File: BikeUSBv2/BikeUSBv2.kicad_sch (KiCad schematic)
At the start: 48 parts, among them J1 TYPE-C-31-M-16, J2 Conn_01x02_Female, Q1 SSM3J332R,LF, Q2 SSM3J332R,LF, SW1 SW_Push, SW2 SW_Push, U1 TPS63020DSJR, U2 ATtiny1616-M

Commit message: added pcb art, other stuff
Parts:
- L1: value 1u -> YPRH0704-1R0M; Alternative (none) -> YPRH0704-2R2M; LCSC Part (none) -> C338840
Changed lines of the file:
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@@
-    (stroke (width 0) (type default))
-  )
-  (wire (pts (xy 78.105 95.885) (xy 70.485 95.885))
     (stroke (width 0) (type default))
   )
@@
   )
   (wire (pts (xy 41.91 88.265) (xy 35.56 88.265))
+    (stroke (width 0) (type default))
+  )
+  (wire (pts (xy 70.485 95.885) (xy 78.105 95.885))
     (stroke (width 0) (type default))
   )
@@
       (effects (font (size 1.27 1.27)))
     )
-    (property "Value" "1u" (at 74.295 100.33 90)
+    (property "Value" "YPRH0704-1R0M" (at 74.295 100.965 90)
       (effects (font (size 1.27 1.27)))
     )
@@
       (effects (font (size 1.27 1.27)) hide)
     )
+    (property "LCSC Part" "C338840" (at 74.295 99.695 90)
+      (effects (font (size 1.27 1.27)) hide)
+    )
+    (property "Alternative" "YPRH0704-2R2M" (at 74.295 99.695 90)
+      (effects (font (size 1.27 1.27)) hide)
+    )

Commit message: small stuff
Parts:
- added TP7: EN, TestPoint:TestPoint_Pad_D2.5mm, symbol Connector:TestPoint
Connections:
- net EN: now also TP7.1
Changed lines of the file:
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@@
+    (stroke (width 0) (type default))
+  )
+  (wire (pts (xy 25.4 172.085) (xy 22.225 172.085))
     (stroke (width 0) (type default))
   )
@@
     (effects (font (size 1.27 1.27)) (justify right bottom))
   )
+  (label "EN" (at 25.4 172.085 180) (fields_autoplaced)
+    (effects (font (size 1.27 1.27)) (justify right bottom))
+  )
   (label "AC1" (at 77.47 111.125 270) (fields_autoplaced)
     (effects (font (size 1.27 1.27)) (justify right bottom))
@@
         )
       )
+    )
+  )
+  (symbol (lib_id "Connector:TestPoint") (at 22.225 172.085 90) (unit 1)
+    (in_bom yes) (on_board yes) (dnp no)
+    (property "Reference" "TP7" (at 20.193 174.625 0)
+      (effects (font (size 1.27 1.27)) (justify right) hide)
+    )
+    (property "Value" "EN" (at 14.605 172.085 90)
+      (effects (font (size 1.27 1.27)) (justify right))
+    )
+    (property "Footprint" "TestPoint:TestPoint_Pad_D2.5mm" (at 22.225 167.005 0)
+      (effects (font (size 1.27 1.27)) hide)
+    )
+    (property "Datasheet" "~" (at 22.225 167.005 0)
+      (effects (font (size 1.27 1.27)) hide)
+    )
+    (pin "1")
+    (instances
+      (project "BikeUSBv2"
+        (path "/b4aff538-5116-4944-9d24-c26a88d7dfe8"
+          (reference "TP7") (unit 1)
+        )
+      )

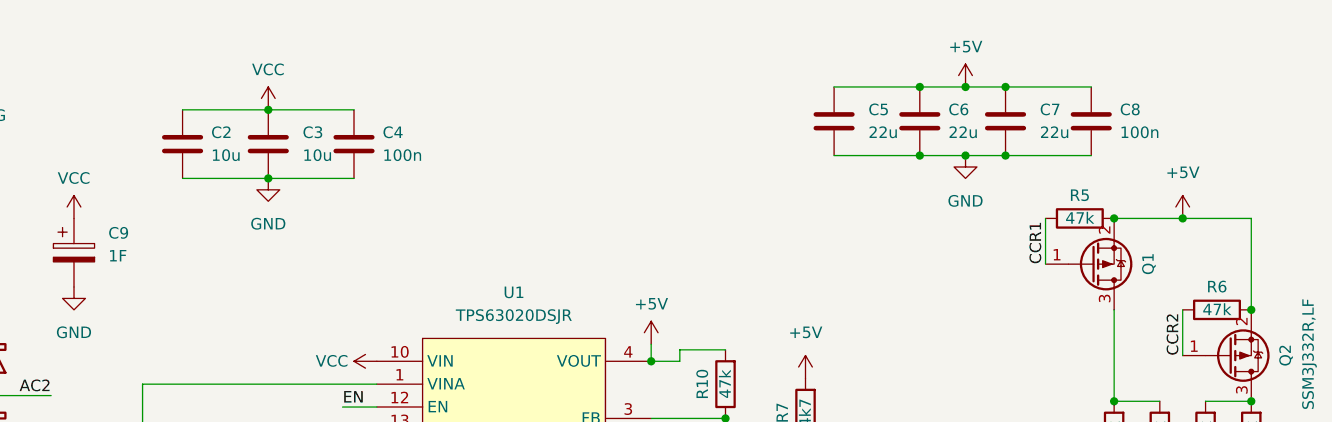
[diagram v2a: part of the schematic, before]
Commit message: better U1 cap layout
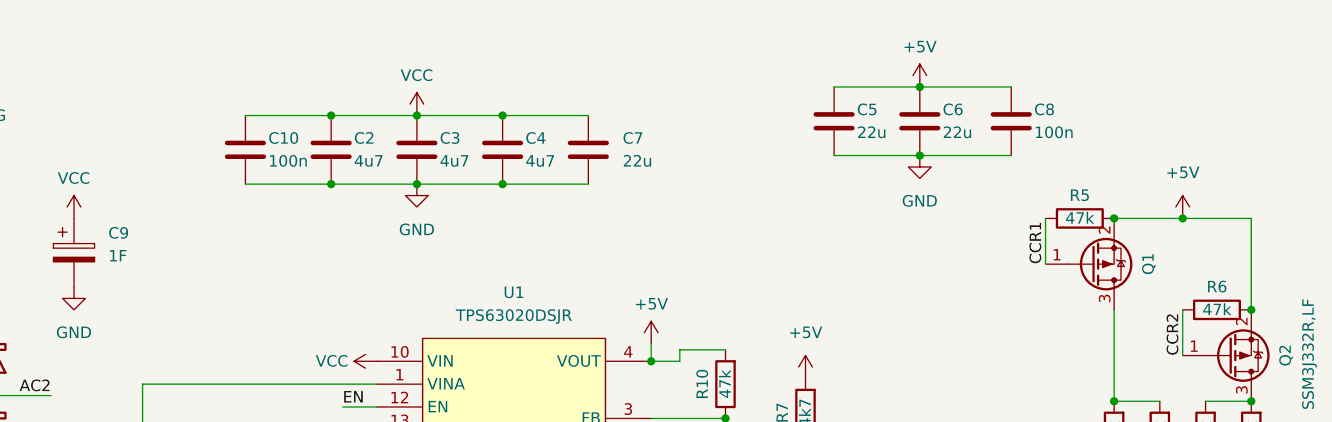
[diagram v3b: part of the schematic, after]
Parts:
- added C10: 100n, Capacitor_SMD:C_0805_2012Metric_Pad1.18x1.45mm_HandSolder, symbol Device:C
- C2, C3: value 10u -> 4u7
- C4: value 100n -> 4u7
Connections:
- net +5V: no longer C7.1
- net GND: now also C10.2
- net VCC: now also C7.1, C10.1
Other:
- moved on the sheet: C2, C3, C4, C8

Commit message: assign some footprints
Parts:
- JP1, TP1, TP2, TP3, TP4, TP5, TP6, TP7: now left out of the parts list
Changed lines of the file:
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@@
   )
   (symbol (lib_id "Connector:TestPoint") (at 24.13 156.21 180) (unit 1)
-    (in_bom yes) (on_board yes) (dnp no)
+    (in_bom no) (on_board yes) (dnp no)
     (property "Reference" "TP3" (at 26.67 158.242 0)
       (effects (font (size 1.27 1.27)) (justify right) hide)
@@
   )
   (symbol (lib_id "Connector:TestPoint") (at 22.225 172.085 90) (unit 1)
-    (in_bom yes) (on_board yes) (dnp no)
+    (in_bom no) (on_board yes) (dnp no)
     (property "Reference" "TP7" (at 20.193 174.625 0)
       (effects (font (size 1.27 1.27)) (justify right) hide)
@@
   )
   (symbol (lib_id "Connector:TestPoint") (at 19.05 157.48 0) (unit 1)
-    (in_bom yes) (on_board yes) (dnp no)
+    (in_bom no) (on_board yes) (dnp no)
     (property "Reference" "TP2" (at 21.59 152.908 0)
       (effects (font (size 1.27 1.27)) (justify left) hide)
@@
   )
   (symbol (lib_id "Connector:TestPoint") (at 29.21 156.21 180) (unit 1)
-    (in_bom yes) (on_board yes) (dnp no)
+    (in_bom no) (on_board yes) (dnp no)
     (property "Reference" "TP6" (at 31.75 158.242 0)
       (effects (font (size 1.27 1.27)) (justify right) hide)
@@
   )
   (symbol (lib_id "Connector:TestPoint") (at 71.12 148.59 270) (unit 1)
-    (in_bom yes) (on_board yes) (dnp no)
+    (in_bom no) (on_board yes) (dnp no)
     (property "Reference" "TP4" (at 76.2 147.32 90)
       (effects (font (size 1.27 1.27)) (justify left) hide)
@@
   )
   (symbol (lib_id "Jumper:SolderJumper_2_Bridged") (at 65.405 96.52 90) (unit 1)
-    (in_bom yes) (on_board yes) (dnp no)
+    (in_bom no) (on_board yes) (dnp no)
     (property "Reference" "JP1" (at 62.865 96.52 0)
       (effects (font (size 1.27 1.27)))
@@
   )
   (symbol (lib_id "Connector:TestPoint") (at 71.12 151.13 270) (unit 1)
-    (in_bom yes) (on_board yes) (dnp no)
+    (in_bom no) (on_board yes) (dnp no)
     (property "Reference" "TP5" (at 77.47 149.86 90)
       (effects (font (size 1.27 1.27)) (justify left) hide)
@@
   )
   (symbol (lib_id "Connector:TestPoint") (at 71.12 146.05 270) (unit 1)
-    (in_bom yes) (on_board yes) (dnp no)
+    (in_bom no) (on_board yes) (dnp no)
     (property "Reference" "TP1" (at 76.2 144.78 90)
       (effects (font (size 1.27 1.27)) (justify left) hide)

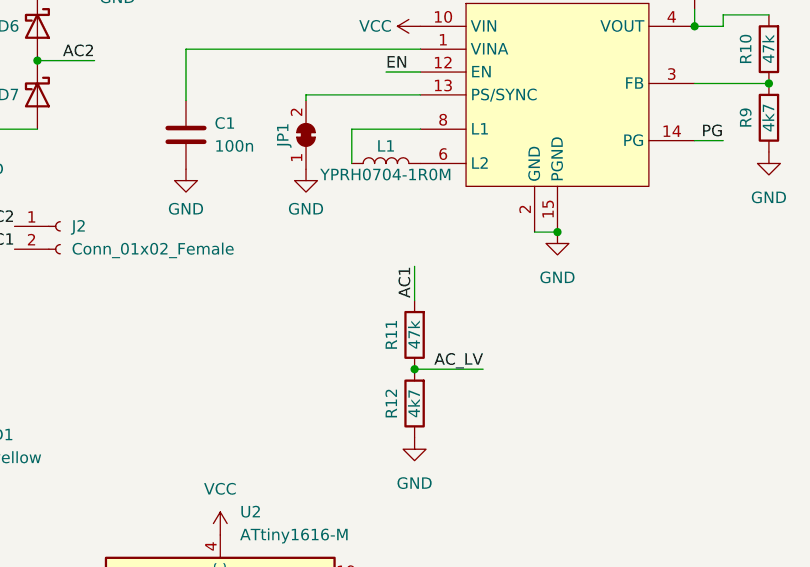
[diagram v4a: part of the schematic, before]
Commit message: switch diode footprints
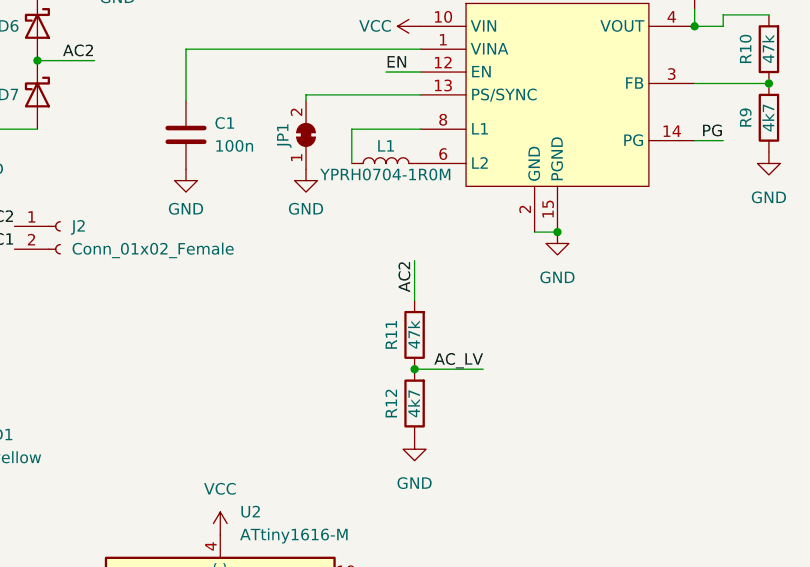
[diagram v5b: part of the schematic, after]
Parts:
- D4, D5, D6, D7: footprint Diode_SMD:D_SOD-128 -> Diode_SMD:D_PowerDI-123
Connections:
- net AC1: no longer R11.2
- net AC2: now also R11.2
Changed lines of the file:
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@@
     (stroke (width 0) (type default))
   )
-  (wire (pts (xy 77.47 111.125) (xy 77.47 114.935))
+  (wire (pts (xy 77.47 110.49) (xy 77.47 114.935))
     (stroke (width 0) (type default))
   )
@@
     (effects (font (size 1.27 1.27)) (justify right bottom))
   )
-  (label "AC1" (at 77.47 111.125 270) (fields_autoplaced)
+  (label "AC2" (at 77.47 110.49 270) (fields_autoplaced)
     (effects (font (size 1.27 1.27)) (justify right bottom))
   )
@@
       (effects (font (size 1.27 1.27)) (justify left) hide)
     )
-    (property "Footprint" "Diode_SMD:D_SOD-128" (at 23.495 84.455 0)
+    (property "Footprint" "Diode_SMD:D_PowerDI-123" (at 23.495 84.455 0)
       (effects (font (size 1.27 1.27)) hide)
     )
@@
       (effects (font (size 1.27 1.27)) (justify left) hide)
     )
-    (property "Footprint" "Diode_SMD:D_SOD-128" (at 35.56 92.075 0)
+    (property "Footprint" "Diode_SMD:D_PowerDI-123" (at 35.56 92.075 0)
       (effects (font (size 1.27 1.27)) hide)
     )
@@
       (effects (font (size 1.27 1.27)) (justify left) hide)
     )
-    (property "Footprint" "Diode_SMD:D_SOD-128" (at 23.495 92.075 0)
+    (property "Footprint" "Diode_SMD:D_PowerDI-123" (at 23.495 92.075 0)
       (effects (font (size 1.27 1.27)) hide)
     )
@@
       (effects (font (size 1.27 1.27)) (justify left) hide)
     )
-    (property "Footprint" "Diode_SMD:D_SOD-128" (at 35.56 84.455 0)
-      (effects (font (size 1.27 1.27)) hide)
-    )
+    (property "Footprint" "Diode_SMD:D_PowerDI-123" (at 35.56 84.455 0)
+      (effects (font (size 1.27 1.27)) hide)
+    )

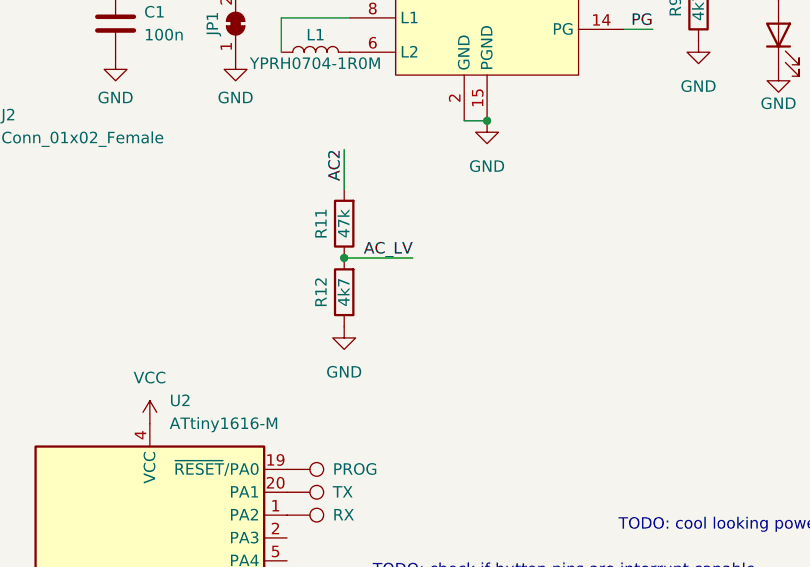
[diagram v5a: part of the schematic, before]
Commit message: added footprint for clamping diode if needed
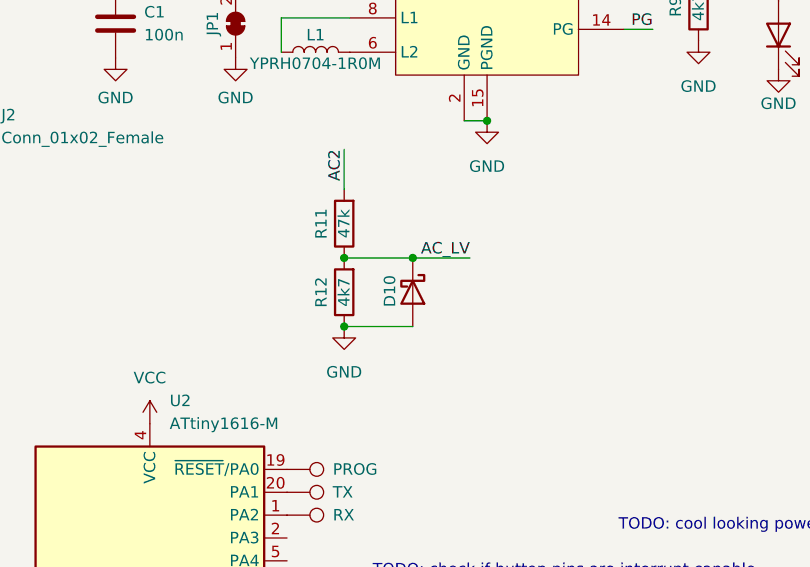
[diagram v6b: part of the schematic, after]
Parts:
- added D10: CMS04(TE12L,Q,M), Diode_SMD:D_PowerDI-123, symbol Device:D_Schottky
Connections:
- net  AC_LV: now also D10.1 (K)
- net GND: now also D10.2 (A)
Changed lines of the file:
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@@
   (junction (at 73.025 64.77) (diameter 0) (color 0 0 0 0)
   )
+  (junction (at 77.47 130.175) (diameter 0) (color 0 0 0 0)
+  )
   (junction (at 92.075 57.15) (diameter 0) (color 0 0 0 0)
   )
@@
   (junction (at 35.56 88.265) (diameter 0) (color 0 0 0 0)
   )
+  (junction (at 85.09 122.555) (diameter 0) (color 0 0 0 0)
+  )
   (junction (at 160.02 68.58) (diameter 0) (color 0 0 0 0)
   )
@@
     (stroke (width 0) (type default))
   )
-  (wire (pts (xy 85.09 122.555) (xy 77.47 122.555))
-    (stroke (width 0) (type default))
-  )
   (wire (pts (xy 170.18 97.79) (xy 170.18 96.52))
     (stroke (width 0) (type default))
@@
     (stroke (width 0) (type default))
   )
+  (wire (pts (xy 77.47 130.175) (xy 85.09 130.175))
+    (stroke (width 0) (type default))
+  )
   (wire (pts (xy 90.805 107.315) (xy 93.345 107.315))
     (stroke (width 0) (type default))
   )
+  (wire (pts (xy 77.47 122.555) (xy 85.09 122.555))
+    (stroke (width 0) (type default))
+  )
   (wire (pts (xy 65.405 92.075) (xy 78.105 92.075))
     (stroke (width 0) (type default))
@@
   )
   (wire (pts (xy 41.91 88.265) (xy 35.56 88.265))
+    (stroke (width 0) (type default))
+  )
+  (wire (pts (xy 85.09 122.555) (xy 91.44 122.555))
     (stroke (width 0) (type default))
   )
@@
     (effects (font (size 1.27 1.27)) (justify right bottom))
   )
-  (label " AC_LV" (at 85.09 122.555 180) (fields_autoplaced)
+  (label " AC_LV" (at 91.44 122.555 180) (fields_autoplaced)
     (effects (font (size 1.27 1.27)) (justify right bottom))
   )
@@
         )
       )
+    )
+  )
+  (symbol (lib_id "Device:D_Schottky") (at 85.09 126.365 270) (unit 1)
+    (in_bom yes) (on_board yes) (dnp no)
+    (property "Reference" "D10" (at 82.55 124.46 0)
+      (effects (font (size 1.27 1.27)) (justify left))
+    )
+    (property "Value" "CMS04(TE12L,Q,M)" (at 81.915 127.635 90)
+      (effects (font (size 1.27 1.27)) (justify left) hide)
+    )
+    (property "Footprint" "Diode_SMD:D_PowerDI-123" (at 85.09 126.365 0)
+      (effects (font (size 1.27 1.27)) hide)
+    )
+    (property "Datasheet" "~" (at 85.09 126.365 0)
+      (effects (font (size 1.27 1.27)) hide)
+    )
+    (property "Sim.Device" "D" (at 85.09 126.365 0)
+      (effects (font (size 1.27 1.27)) hide)
+    )
+    (property "Sim.Pins" "1=K 2=A" (at 85.09 126.365 0)
+      (effects (font (size 1.27 1.27)) hide)
+    )
+    (pin "2")
+    (pin "1")
+    (instances
+      (project "BikeUSBv2"
+        (path "/b4aff538-5116-4944-9d24-c26a88d7dfe8"
+          (reference "D10") (unit 1)
+        )
+      )
